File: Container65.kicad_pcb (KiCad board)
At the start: 2 copper layers, 76.2 x 100 mm, 91 parts, among them J1 Conn_01x03, J2 Conn_01x06, J3 POGOm1, J4 POGOm2, J5 POGOf1, J6 POGOf2, SW1 RotaryEncoder_Switch, U1 RP2040, U2 TYPE-C-31-M-12, U3 XC6206PxxxMR, U4 W25Q128JVS, U5 USB Boot, U6 Reset, U7 TRRS, Y1 12MHz - 20pF

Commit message: Finished routing MCU
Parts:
- removed J2: Conn_01x06, Connector_PinHeader_1.27mm:PinHeader_1x06_P1.27mm_Vertical
- added D23: 1N4148W, Keebio-Parts:D_SOD123, B.Cu at (102.4, 54.0)
- added R10: 4.7k, Keebio-Parts:R_0402, B.Cu at (97.3, 34.8)
- added R11: 4.7k, Keebio-Parts:R_0402, B.Cu at (97.3, 36.8)
- J3: footprint extras:1x02_2.54_Pogo Male GND -> Extras:1x02_2.54_Pogo Male GND; moved to B.Cu
- J4: footprint extras:1x02_2.54_Pogo Male -> Extras:1x02_2.54_Pogo Male; moved to B.Cu
- J5: footprint extras:1x02_2.54_Pogo Female GND -> Extras:1x02_2.54_Pogo Female GND; moved to B.Cu
- J6: footprint extras:1x02_2.54_Pogo Female -> Extras:1x02_2.54_Pogo Female; moved to B.Cu
- R1, R2: footprint Keebio-Parts:R_0402 -> Keebio-Parts:R_0603
- U1: footprint extras:rp2040 -> Extras:rp2040
- U2: footprint extras:simple-usb-c -> Extras:simple-usb-c
- U5, U6: footprint extras:tactile-switch -> Extras:3x4x2.5mm Micro Switch
- U7: moved to B.Cu
- moved R4 137.5 mm to (103.2, 36.6)
- moved C18 126.6 mm to (62.5, 39.8), turned to -90 degrees
- moved C14 119.8 mm to (89.5, 27.0)
- moved C2 114.0 mm to (73.6, 28.6)
- moved R8 100.0 mm to (62.7, 37.2), turned to 0 degrees
- moved R6 99.1 mm to (61.7, 34.2), turned to 0 degrees
- moved C10 98.8 mm to (70.7, 33.4)
- moved J1 85.2 mm to (71.0, 39.4), turned to 90 degrees
- moved F1 81.8 mm to (51.9, 36.2), turned to 0 degrees
- moved Y1 74.8 mm to (87.4, 38.5)
- moved R7 73.9 mm to (55.9, 34.2)
- moved C15 71.5 mm to (70.7, 32.2)
- moved U3 68.8 mm to (89.5, 34.4)
- moved R1 68.7 mm to (65.5, 30.6), turned to -90 degrees
- moved FB1 66.5 mm to (88.3, 31.6), turned to 0 degrees
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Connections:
- J3 pad 2: VCC -> +3V3
- J4 pad 1: SDA -> SCL
- J4 pad 2: SCL -> SDA
- J5 pad 2: VCC -> +3V3
- J6 pad 1: SDA -> SCL
- J6 pad 2: SCL -> SDA
- OL1 pad 3: VCC -> +3V3
- SW1 pad A: unconnected-(SW1-PadA) -> encB
- SW1 pad B: unconnected-(SW1-PadB) -> encA
- SW1 pad C: unconnected-(SW1-PadC) -> GND
- SW1 pad S1: unconnected-(SW1-PadS1) -> Net-(D23-Pad2)
- SW1 pad S2: unconnected-(SW1-PadS2) -> COL3
- U1 pad 13: CLM5 -> COL3
- U1 pad 14: CLM7 -> ROW0
- U1 pad 38: SCK -> unconnected-(U1-Pad38)
- U1 pad 39: MOSI -> unconnected-(U1-Pad39)
- U1 pad 40: MISO -> unconnected-(U1-Pad40)
- U1 pad 41: CS -> unconnected-(U1-Pad41)
- U2 pad 0: unconnected-(U2-Pad0) -> GND
- U7 pad 2: VCC -> +3V3
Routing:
- net +3V3: track 0.00 -> 143.8 mm, vias 0 -> 6
- net GND: track 0.00 -> 89.1 mm, vias 0 -> 31
- net SCL: track 0.00 -> 56.2 mm, vias 0 -> 1
- net QSPI_SD3: track 0.00 -> 43.8 mm
- net Net-(F1-Pad2): track 0.00 -> 40.7 mm, vias 0 -> 2
- net QSPI_SCLK: track 0.00 -> 40.7 mm
- net QSPI_SD0: track 0.00 -> 37.4 mm
- net QSPI_SS: track 0.00 -> 29.9 mm
- net +1V1: track 0.00 -> 28.2 mm
- net QSPI_SD1: track 0.00 -> 26.9 mm
- net QSPI_SD2: track 0.00 -> 26.0 mm
- net RUN: track 0.00 -> 19.8 mm
- net USB-: track 0.00 -> 18.6 mm
- net OSC_OUT: track 0.00 -> 18.4 mm
- net USB+: track 0.00 -> 17.1 mm
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- added copper zone on B.Cu, net GND
- added copper zone on F.Cu, net GND
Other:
- board size 76.2 x 100 mm -> 76.2 x 108.7 mm

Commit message: Finished routing
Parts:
- moved D17 25.4 mm to (46.0, 129.4)
- moved D20 25.4 mm to (109.5, 129.4)
- moved D3 12.7 mm to (90.5, 54.0)
- moved D1 7.14 mm to (60.3, 54.0)
- moved D2 7.14 mm to (64.3, 54.0)
- moved D23 7.14 mm to (109.5, 54.0)
- moved D4 3.17 mm to (95.2, 54.0)
- moved J4 3.00 mm to (37.2, 55.5)
- moved J6 3.00 mm to (118.4, 55.5)
- moved J3 3.00 mm to (37.2, 93.5)
- moved J5 3.00 mm to (118.4, 93.5)
- moved C11 1.72 mm to (78.1, 41.2), turned to -90 degrees
- moved C10 0.80 mm to (69.9, 33.4)
- moved D11 0.79 mm to (90.5, 92.1)
- moved D15 0.79 mm to (90.5, 111.1)
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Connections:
- J4 pad 1: SCL -> SDA
- J4 pad 2: SDA -> SCL
- J6 pad 1: SCL -> SDA
- J6 pad 2: SDA -> SCL
- MX-E-1 pad 1: COL3 -> COL0
- MX-E-1 pad 2: Net-(D8-Pad2) -> Net-(D5-Pad2)
- MX-E-3 pad 1: COL3 -> COL0
- MX-E-3 pad 2: Net-(D16-Pad2) -> Net-(D13-Pad2)
- MX-E-4 pad 1: COL2 -> COL3
- MX-E-4 pad 2: Net-(D19-Pad2) -> Net-(D20-Pad2)
- MX17 pad 1: COL0 -> COL1
- R10 pad 2: SDA -> SCL
- R11 pad 2: SCL -> SDA
- U1 pad 14: ROW0 -> unconnected-(U1-Pad14)
- U1 pad 15: CLM8 -> unconnected-(U1-Pad15)
- U1 pad 16: CLM9 -> unconnected-(U1-Pad16)
- U1 pad 17: CLM10 -> unconnected-(U1-Pad17)
- U1 pad 18: ROW4 -> unconnected-(U1-Pad18)
- U1 pad 27: CLM1 -> unconnected-(U1-Pad27)
- U1 pad 28: CLM2 -> unconnected-(U1-Pad28)
- U1 pad 29: CLM3 -> ROW2
- U1 pad 30: CLM6 -> ROW3
- U1 pad 31: CLM11 -> ROW4
- U1 pad 32: unconnected-(U1-Pad32) -> COL2
- U1 pad 34: CLM12 -> ROW1
- U1 pad 35: CLM13 -> ROW0
- U1 pad 36: ROW5 -> COL1
- U1 pad 37: ROW1 -> COL0
- U1 pad 8: unconnected-(U1-Pad8) -> encA
- U1 pad 9: unconnected-(U1-Pad9) -> encB
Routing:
- net ROW4: track 0.00 -> 164.3 mm, vias 0 -> 2
- net COL1: track 0.00 -> 128.3 mm, vias 0 -> 10
- net +3V3: track 143.8 -> 271.1 mm, vias 6 -> 9
- net COL3: track 0.00 -> 122.8 mm, vias 0 -> 8
- net ROW3: track 0.00 -> 115.5 mm, vias 0 -> 2
- net COL0: track 0.00 -> 114.1 mm, vias 0 -> 4
- net SDA: track 17.1 -> 129.8 mm, vias 1 -> 2
- net COL2: track 0.00 -> 97.5 mm, vias 0 -> 10
- net ROW2: track 0.00 -> 95.9 mm, vias 0 -> 2
- net ROW1: track 0.00 -> 88.5 mm, vias 0 -> 2
- net ROW0: track 0.00 -> 77.7 mm, vias 0 -> 2
- net SCL: track 56.2 -> 115.0 mm
- net Net-(D20-Pad2): track 0.00 -> 43.0 mm
- net encB: track 0.00 -> 39.8 mm, vias 0 -> 3
- net encA: track 0.00 -> 38.1 mm, vias 0 -> 3
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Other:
- board size 76.2 x 108.7 mm -> 78.7 x 108.7 mm

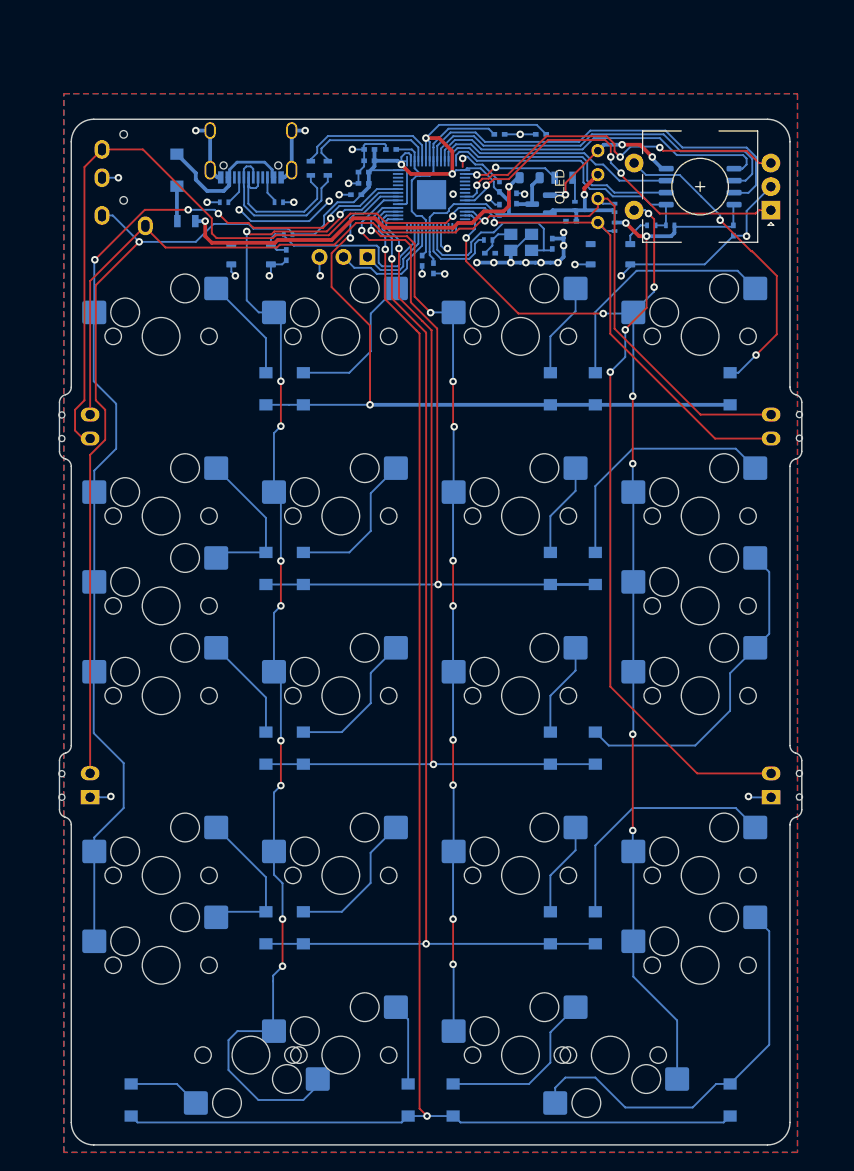
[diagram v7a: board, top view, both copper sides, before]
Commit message: More routing fix
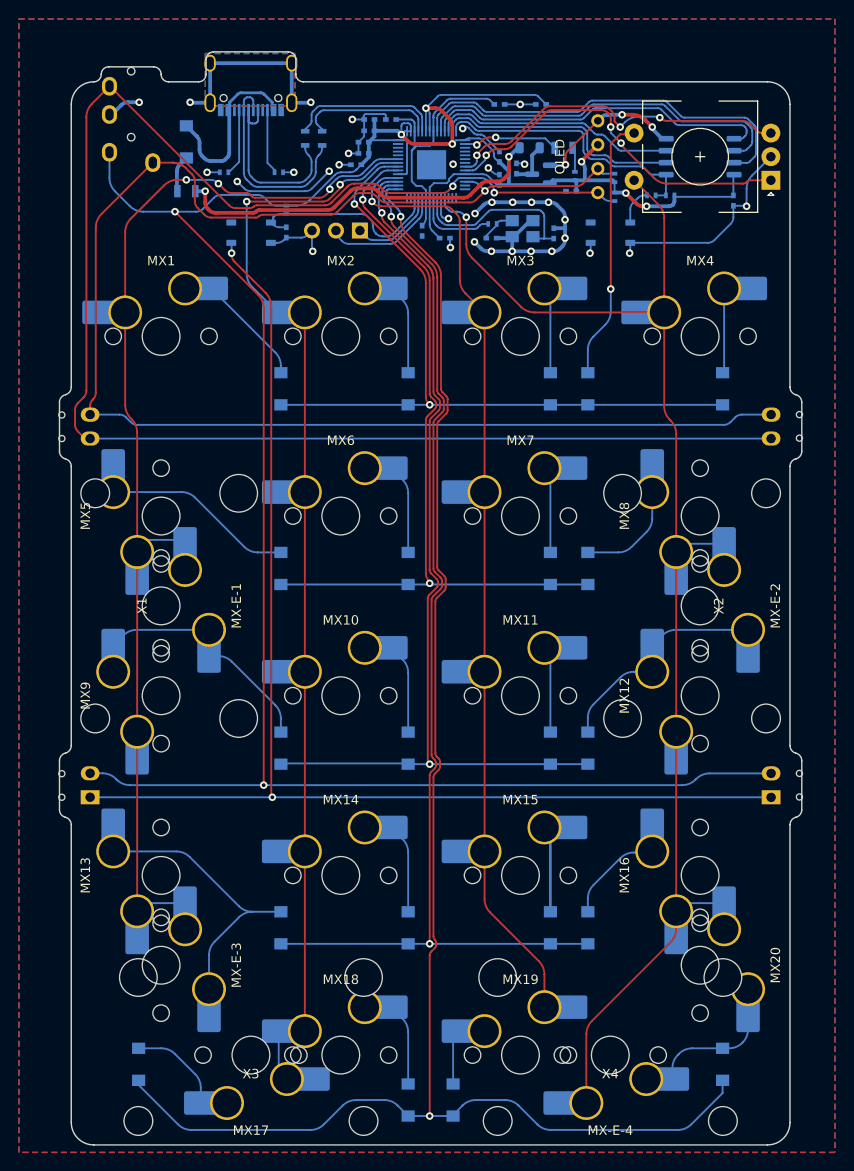
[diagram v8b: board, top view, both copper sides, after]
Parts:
- added X1: 2u Stabilizer, Mounting_Keyboard_Stabilizer:Stabilizer_Cherry_MX_2.00u, F.Cu at (49.2, 77.0)
- added X2: 2u Stabilizer, Mounting_Keyboard_Stabilizer:Stabilizer_Cherry_MX_2.00u, F.Cu at (106.4, 77.0)
- added X3: 2u Stabilizer, Mounting_Keyboard_Stabilizer:Stabilizer_Cherry_MX_2.00u, F.Cu at (58.7, 124.6)
- added X4: 2u Stabilizer, Mounting_Keyboard_Stabilizer:Stabilizer_Cherry_MX_2.00u, F.Cu at (96.8, 124.6)
- MX-E-1, MX-E-2, MX-E-3, MX-E-4, MX17, MX20: footprint Switch_Keyboard_Hotswap_Kailh:SW_Hotswap_Kailh_MX_1.00u_Extras -> Switch_Keyboard_Hotswap_Kailh:SW_Hotswap_Kailh_MX_plated_2.00u_Modified
- MX1, MX10, MX11, MX12, MX13, MX14, MX15, MX16, MX18, MX19, MX2, MX3, MX4, MX5, MX6, MX7, MX8, MX9: footprint Switch_Keyboard_Hotswap_Kailh:SW_Hotswap_Kailh_MX_1.00u_Modified -> Switch_Keyboard_Hotswap_Kailh:SW_Hotswap_Kailh_MX_plated_1.00u_Modified
- moved D23 15.1 mm to (94.5, 54.0)
- moved D4 13.5 mm to (108.7, 54.0)
- moved D10 11.1 mm to (75.4, 92.1)
- moved D14 11.1 mm to (75.4, 111.1)
- moved D2 11.1 mm to (75.4, 54.0)
- moved D6 11.1 mm to (75.4, 73.0)
- moved U2 7.14 mm to (58.7, 20.6)
- moved U7 6.75 mm to (46.0, 18.7)
- moved D17 3.86 mm to (46.8, 125.6)
- moved D20 3.86 mm to (108.7, 125.6)
- moved C11 3.42 mm to (79.3, 38.0), turned to 0 degrees
- moved R1 3.23 mm to (64.5, 27.4)
- moved R2 3.23 mm to (66.3, 27.4)
- moved C13 3.18 mm to (85.1, 29.4)
- moved C15 3.18 mm to (70.7, 29.0)
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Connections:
- MX-E-1 pad 2: Net-(D5-Pad2) -> Net-(D9-Pad2)
- MX-E-4 pad 1: COL3 -> Net-(D20-Pad2)
- MX-E-4 pad 2: Net-(D20-Pad2) -> COL3
- MX19 pad 1: COL2 -> Net-(D19-Pad2)
- MX19 pad 2: Net-(D19-Pad2) -> COL2
- U1 pad 13: COL3 -> unconnected-(U1-Pad13)
- U1 pad 18: unconnected-(U1-Pad18) -> COL3
- U1 pad 29: ROW2 -> ROW4
- U1 pad 31: ROW4 -> ROW2
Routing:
- net GND: track 124.6 -> 274.0 mm, vias 37 -> 38
- net SCL: track 115.0 -> 160.3 mm
- net SDA: track 129.8 -> 173.9 mm
- net Net-(D20-Pad2): track 43.0 -> 12.3 mm
- net COL3: track 122.8 -> 144.7 mm, vias 8 -> 1
- net Net-(D4-Pad2): track 26.0 -> 9.00 mm
- net Net-(D16-Pad2): track 26.5 -> 10.7 mm
- net COL1: track 128.3 -> 112.6 mm, vias 10 -> 2
- net Net-(D8-Pad2): track 26.5 -> 11.4 mm
- net Net-(D13-Pad2): track 16.6 -> 30.6 mm
- net Net-(D12-Pad2): track 34.9 -> 21.4 mm
- net Net-(D19-Pad2): track 18.2 -> 5.83 mm
- net Net-(D9-Pad2): track 11.1 -> 22.8 mm
- net +3V3: track 271.1 -> 281.6 mm, vias 9 -> 8
- net ROW4: track 164.3 -> 174.4 mm
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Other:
- board size 78.7 x 108.7 mm -> 78.7 x 115.9 mm
